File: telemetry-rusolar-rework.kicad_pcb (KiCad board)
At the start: 4 copper layers, 108.1 x 81.6 mm, 132 parts, among them IC1 TLV62569DBVR, J10 JP, J11 USB_B_Micro, J13 GR2, J14 GR1, J15 N_GR1, J19 Micro_SD_Card, J2 SPI, J3 MDT420E01001, J4 CAN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

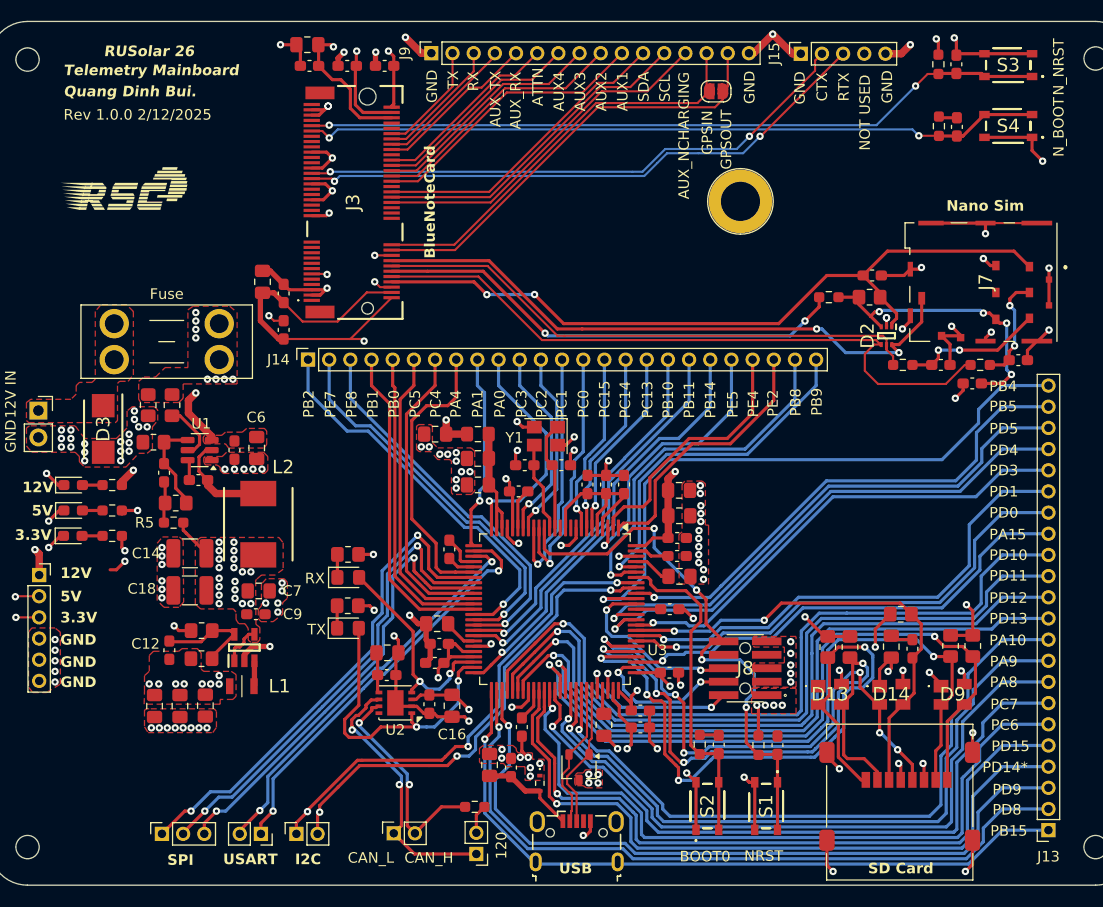
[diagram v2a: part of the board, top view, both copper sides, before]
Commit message: Fixed DRC errors
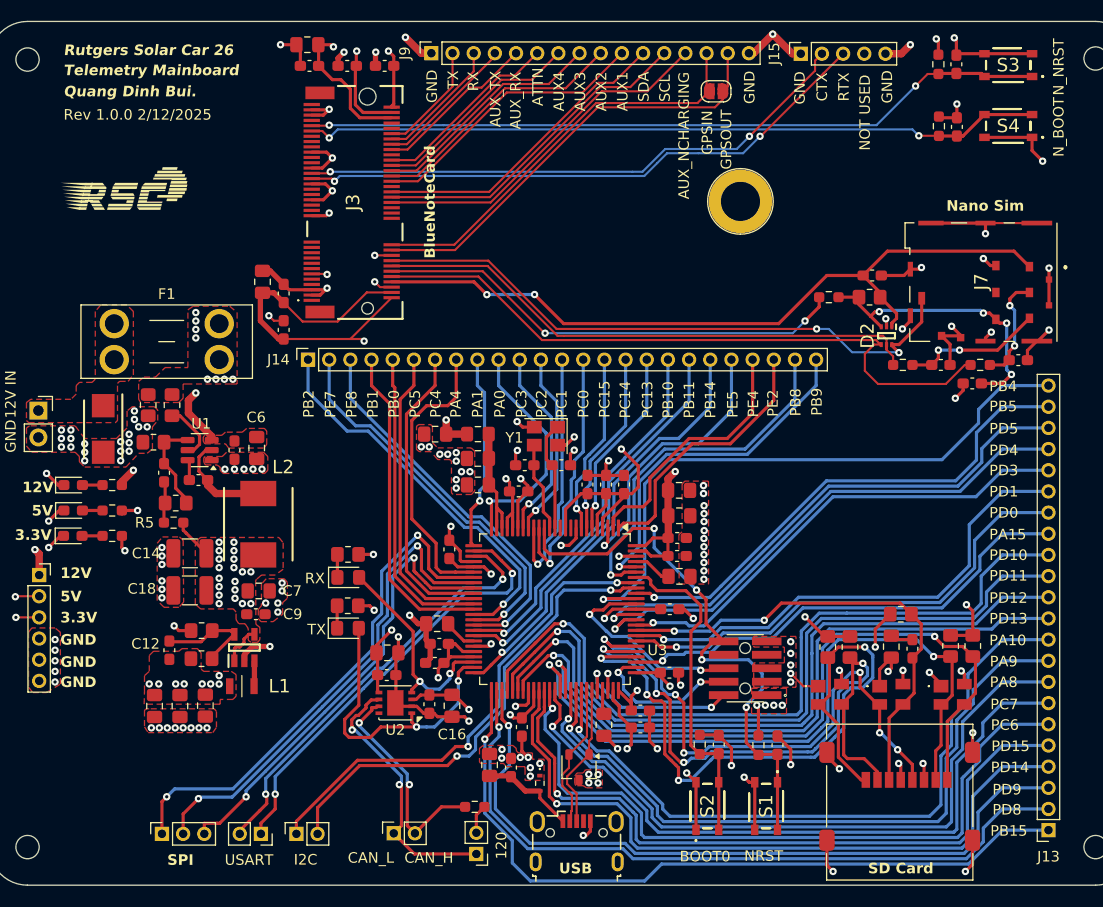
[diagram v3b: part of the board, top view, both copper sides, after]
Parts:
- renumbered Fuse to F1, USART to J1, I2C to J12
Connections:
- net PD14* renamed /PD14
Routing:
- net +3.3V Buck: track 153.9 -> 170.5 mm, vias 33 -> 38
- net GND: track 201.1 -> 212.4 mm, vias 149 -> 150
- net /USART2_TX: track 39.2 -> 41.8 mm
- net /PB15: track 68.4 -> 71.0 mm
- net /USART2_RX: track 38.3 -> 40.5 mm
- net /SWO: track 17.7 -> 19.7 mm
- net /SPI1_SCK: track 47.8 -> 49.6 mm
- net /NRST: track 53.0 -> 54.1 mm
- net /SPI1_MISO: track 45.1 -> 46.1 mm
- net /I2C1_SDA: vias 3 -> 2
- net /I2C1_SCL: vias 3 -> 2
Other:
- board text added: "I2C"
- board text added: "PD14"
- board text added: "Rutgers Solar Car 26"
- board text added: "USART"
- board text removed: "PD14*"
- board text removed: "RUSolar 26"

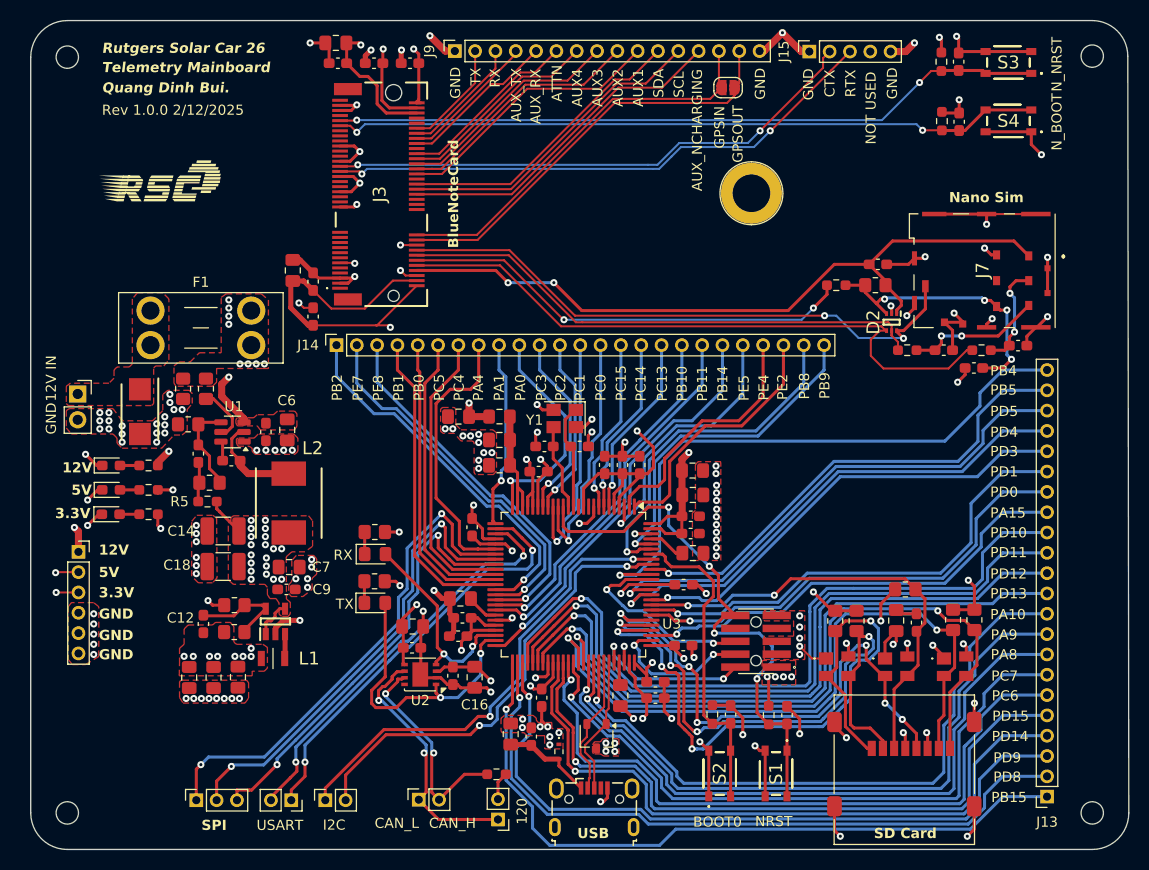
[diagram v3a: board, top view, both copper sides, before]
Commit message: Added ORing VBUS
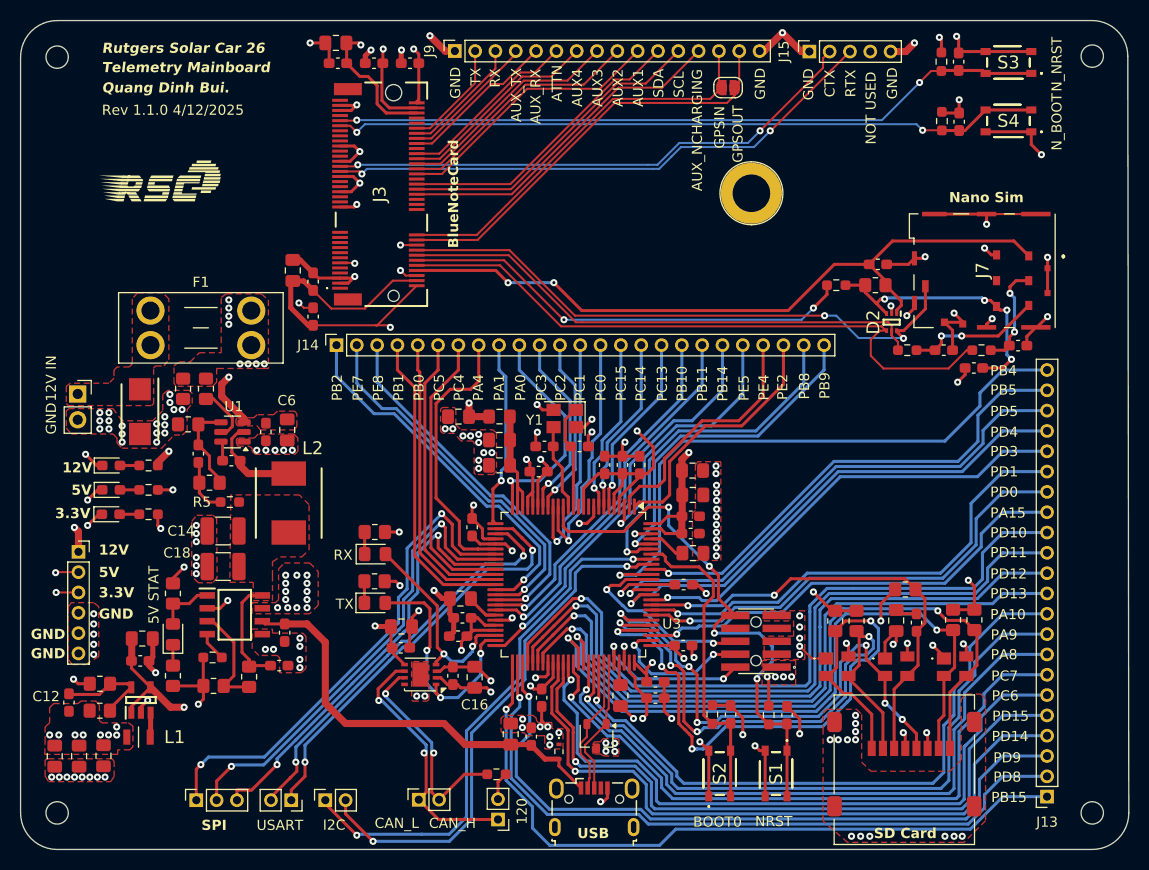
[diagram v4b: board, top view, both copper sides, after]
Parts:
- added C60: 100n, Capacitor_SMD:C_0603_1608Metric_Pad1.08x0.95mm_HandSolder, F.Cu at (45.5, 159.5)
- added C61: 100n, Capacitor_SMD:C_0603_1608Metric_Pad1.08x0.95mm_HandSolder, F.Cu at (46.0, 156.3)
- added D4: 5V_S, LED_SMD:LED_0805_2012Metric_Pad1.15x1.40mm_HandSolder, F.Cu at (35.0, 156.4)
- added IC2: TPS2113APW, SamacSys_Parts:NE555DR, F.Cu at (41.1, 154.5)
- added R10: 36k, Resistor_SMD:R_0805_2012Metric_Pad1.20x1.40mm_HandSolder, F.Cu at (39.0, 161.5)
- added R11: 500, Resistor_SMD:R_0603_1608Metric_Pad0.98x0.95mm_HandSolder, F.Cu at (38.9, 158.7)
- added R12: 10k, Resistor_SMD:R_0805_2012Metric_Pad1.20x1.40mm_HandSolder, F.Cu at (35.0, 152.4)
- added R31: 2k2, Resistor_SMD:R_0805_2012Metric_Pad1.20x1.40mm_HandSolder, F.Cu at (35.0, 160.5)
- added R9: 157k, Resistor_SMD:R_0805_2012Metric_Pad1.20x1.40mm_HandSolder, F.Cu at (42.5, 160.6)
- moved C7 16.1 mm to (32.0, 156.8)
- moved C9 16.0 mm to (31.8, 159.0)
- moved R6 15.3 mm to (27.8, 163.9)
- moved C21 15.3 mm to (28.2, 168.4)
- moved C12 15.3 mm to (24.8, 163.1)
- moved C15 15.3 mm to (23.4, 168.4)
- moved C20 15.3 mm to (25.8, 168.4)
- moved L1 15.3 mm to (31.6, 166.5)
- moved IC1 15.3 mm to (31.9, 162.9)
- moved R14 15.3 mm to (27.8, 161.3)
- moved R5 2.20 mm to (40.6, 143.4)
- moved C58 1.10 mm to (57.4, 157.8)
- moved C59 1.10 mm to (57.5, 155.7)
- moved H1 1.00 mm to (23.6, 99.6)
- moved H2 1.00 mm to (23.6, 174.0)
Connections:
- C26 pad 2: +5V Buck -> +5V
- C28 pad 2: +5V Buck -> +5V
- C29 pad 2: +5V Buck -> +5V
- C50 pad 2: +5V Buck -> +5V
- C7 pad 2: +5V Buck -> +5V
- C9 pad 1: +5V Buck -> +5V
- IC1 pad 1: +5V Buck -> +5V
- IC1 pad 4: +5V Buck -> +5V
- J3 pad 70: +5V Buck -> +5V
- J3 pad 72: +5V Buck -> +5V
- J3 pad 74: +5V Buck -> +5V
- J5 pad 2: +5V Buck -> +5V
- R29 pad 1: +5V Buck -> +5V
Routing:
- net +5V: track 0.00 -> 47.5 mm, vias 0 -> 20
- net VBUS: track 9.09 -> 42.1 mm
- net +5V Buck: track 40.1 -> 11.0 mm, vias 24 -> 0
- net Net-(IC2-VSNS): track 0.00 -> 10.7 mm
- net /I2C1_SCL: track 45.2 -> 52.1 mm
- net /I2C1_SDA: track 46.4 -> 53.2 mm
- net Net-(D4-A): track 0.00 -> 5.71 mm
- net /CAN2_TX: track 28.7 -> 25.0 mm, vias 2 -> 3
- net Net-(IC2-ILIM): track 0.00 -> 2.90 mm
- net Net-(D4-K): track 0.00 -> 2.05 mm
- net GND: track 212.4 -> 210.5 mm, vias 150 -> 165
- net Net-(C19-Pad1): track 3.94 -> 5.66 mm
- net +3.3V Buck: track 170.5 -> 169.8 mm
- net /SD1_D3: track 58.6 -> 58.0 mm
- added copper zone on F.Cu, net +5V
- added copper zone on In2.Cu, net +5V
- removed copper zone on In2.Cu, net +5V Buck
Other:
- board size 108.1 x 81.6 mm -> 109.1 x 81.6 mm
- board text added: "5V STAT"
- board text added: "Rev 1.1.0 4/12/2025"
- board text added: "https://github.com/bquangDinh/telemetry-board-rework"
- board text removed: "Rev 1.0.0 2/12/2025"

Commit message: Removed CAN TX/RX LED indicators
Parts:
- removed D5: TX, LED_SMD:LED_0805_2012Metric_Pad1.15x1.40mm_HandSolder
- removed D6: RX, LED_SMD:LED_0805_2012Metric_Pad1.15x1.40mm_HandSolder
- removed R7, R8: 1k5, Resistor_SMD:R_0805_2012Metric_Pad1.20x1.40mm_HandSolder
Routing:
- net /CAN2_TX: track 25.0 -> 10.2 mm, vias 3 -> 2
- net /CAN2_RX: track 20.6 -> 7.04 mm, vias 2 -> 0
- net +3.3V Buck: track 169.8 -> 176.7 mm
- net GND: track 210.5 -> 207.5 mm, vias 165 -> 163
- net Net-(D6-K): track 2.18 -> 0.00 mm
- net Net-(D5-K): track 2.12 -> 0.00 mm
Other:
- board text added: "Rev 1.1.1 4/12/2025"
- board text removed: "Rev 1.1.0 4/12/2025"

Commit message: Added LED indicators, USER LEDs, extended layout, fixed footprints
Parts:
- removed J19: Micro_SD_Card, Connector_Card:microSD_HC_Molex_47219-2001
- added C62: 100n, Capacitor_SMD:C_0603_1608Metric_Pad1.08x0.95mm_HandSolder, F.Cu at (83.4, 173.6)
- added D15: CAN_ERR, LED_SMD:LED_0805_2012Metric_Pad1.15x1.40mm_HandSolder, F.Cu at (53.5, 138.3)
- added D16: USER LED 1, LED_SMD:LED_0805_2012Metric_Pad1.15x1.40mm_HandSolder, F.Cu at (91.4, 142.1)
- added D17: USER LED 2, LED_SMD:LED_0805_2012Metric_Pad1.15x1.40mm_HandSolder, F.Cu at (91.4, 146.8)
- added D5: CAN_PWR, LED_SMD:LED_0805_2012Metric_Pad1.15x1.40mm_HandSolder, F.Cu at (53.7, 152.1)
- added D6: TX, LED_SMD:LED_0805_2012Metric_Pad1.15x1.40mm_HandSolder, F.Cu at (53.6, 147.4)
- added D7: RX, LED_SMD:LED_0805_2012Metric_Pad1.15x1.40mm_HandSolder, F.Cu at (53.6, 142.9)
- added FB1: FerriteBead, Inductor_SMD:L_0805_2012Metric_Pad1.05x1.20mm_HandSolder, F.Cu at (83.8, 175.5)
- added J16: 47219-2001, SamacSys_Parts:472192001, F.Cu at (106.1, 170.9)
- added R32: 1k5, Resistor_SMD:R_0603_1608Metric_Pad0.98x0.95mm_HandSolder, F.Cu at (55.8, 142.9)
- added R33: 1k5, Resistor_SMD:R_0603_1608Metric_Pad0.98x0.95mm_HandSolder, F.Cu at (55.8, 138.3)
- added R34: 1k5, Resistor_SMD:R_0603_1608Metric_Pad0.98x0.95mm_HandSolder, F.Cu at (92.9, 140.1)
- added R35: 1k5, Resistor_SMD:R_0603_1608Metric_Pad0.98x0.95mm_HandSolder, F.Cu at (92.9, 144.8)
- added R7: 1k5, Resistor_SMD:R_0603_1608Metric_Pad0.98x0.95mm_HandSolder, F.Cu at (55.8, 152.1)
- added R8: 1k5, Resistor_SMD:R_0603_1608Metric_Pad0.98x0.95mm_HandSolder, F.Cu at (55.8, 147.4)
- D10, D11, D12: footprint LED_SMD:LED_0603_1608Metric_Pad1.05x0.95mm_HandSolder -> LED_SMD:LED_0805_2012Metric_Pad1.15x1.40mm_HandSolder
- moved J11 2.80 mm to (76.5, 176.2)
- moved H2 2.50 mm to (23.6, 176.5)
- moved H3 2.50 mm to (125.5, 176.5)
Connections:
- net /PA4 renamed /PA4*
- net /PB1 renamed /PB1*
- net /PB2 renamed /PB2*
- net /PB5 renamed /PB5*
- net /PE2 renamed /PE2*
- J11 pad 6: unconnected-(J11-Shield-Pad6) -> Net-(J11-Shield)
- J14 pad 18: /PB10 -> PB10
- J14 pad 19: /PB11 -> PB11
- J14 pad 21: /PE5 -> PE5
- J3 pad 54: /blue-note-card/ATTN -> PE5
- J3 pad 62: /blue-note-card/RX -> PB10
- J3 pad 64: /blue-note-card/TX -> PB11
- J9 pad 2: /blue-note-card/TX -> PB11
- J9 pad 3: /blue-note-card/RX -> PB10
- J9 pad 6: /blue-note-card/ATTN -> PE5
- U3 pad 3: /PE5 -> PE5
- U3 pad 42: /PB10 -> PB10
- U3 pad 43: /PB11 -> PB11
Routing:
- net PB11: track 0.00 -> 101.0 mm, vias 0 -> 2
- net PB10: track 0.00 -> 98.4 mm, vias 0 -> 2
- net PE5: track 0.00 -> 95.4 mm, vias 0 -> 2
- net /PB11: track 37.2 -> 0.00 mm, vias 1 -> 0
- net /PB10: track 35.3 -> 0.00 mm, vias 1 -> 0
- net /PE5: track 26.3 -> 0.00 mm, vias 1 -> 0
- net Net-(J11-Shield): track 0.00 -> 20.1 mm
- net /blue-note-card/ATTN: track 17.9 -> 0.00 mm
- net +3.3V Buck: track 176.7 -> 191.3 mm
- net /blue-note-card/RX: track 12.1 -> 0.00 mm
- net /PA4*: track 27.2 -> 39.0 mm, vias 0 -> 2
- net /blue-note-card/TX: track 10.7 -> 0.00 mm
- net /PB2*: track 37.1 -> 46.5 mm, vias 1 -> 2
- net GND: track 207.5 -> 216.3 mm, vias 163 -> 176
- net /PE2*: track 25.4 -> 32.9 mm
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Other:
- board size 109.1 x 81.6 mm -> 109.1 x 84.1 mm
- board text added: "CAN_ERR"
- board text added: "CAN_PWR"
- board text added: "PA4*"
- board text added: "PA4* -> CAN_ERR"
- board text added: "PB1*"
- board text added: "PB1* -> TX"
- board text added: "PB10*"
- board text added: "PB10* -> USART3 TX"
- board text added: "PB11*"
- board text added: "PB11* -> USART3 RX"
- board text added: "PB2*"
- board text added: "PB2* -> RX"
- board text added: "PB5*"
- board text added: "PE2*"
- board text added: "PE2* -> USER LED 1"
- board text added: "PE5*"
- board text added: "PE5* -> USER LED 2"
- board text added: "SWD"
- board text added: "USER LED 1"
- board text added: "USER LED 2"
- board text added: "VBUS"
- board text removed: "PA4"
- board text removed: "PB1"
- board text removed: "PB10"
- board text removed: "PB11"
- board text removed: "PB2"
- board text removed: "PB5"
- board text removed: "PE2"
- board text removed: "PE5"

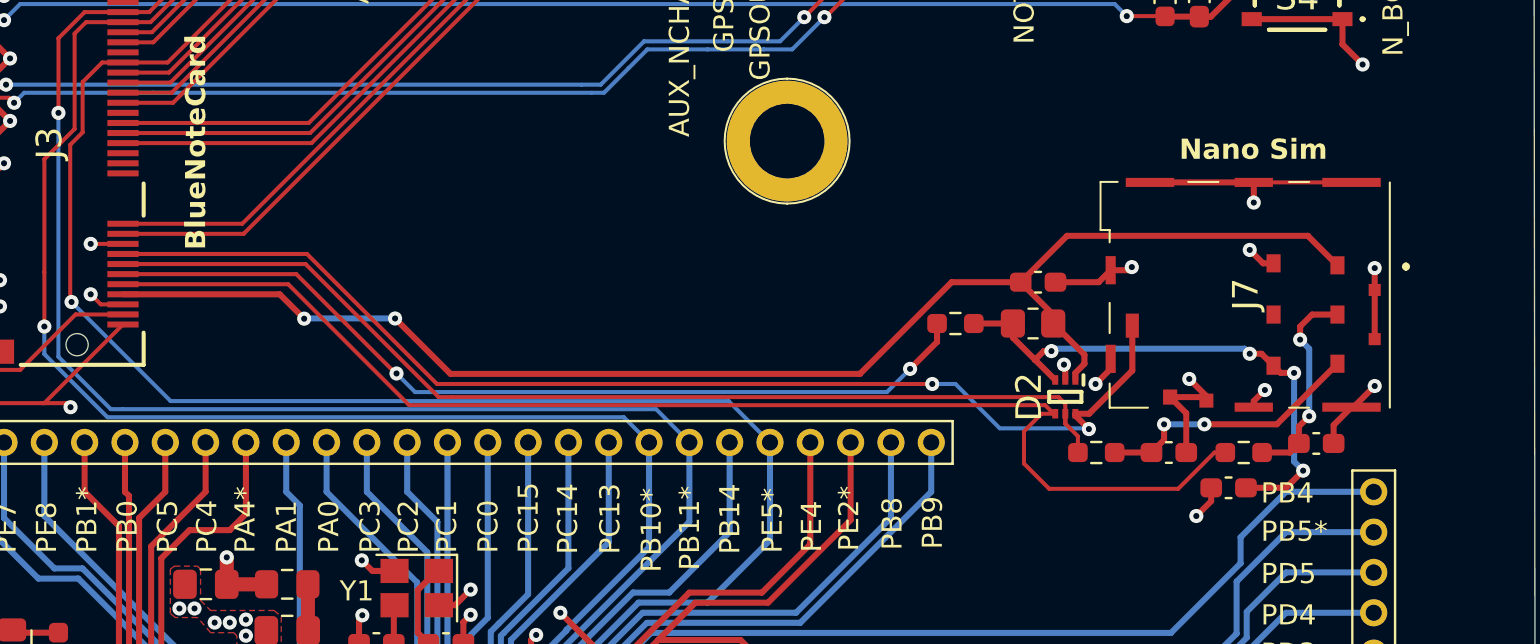
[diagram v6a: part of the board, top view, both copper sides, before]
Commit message: Relayout NanoSim component
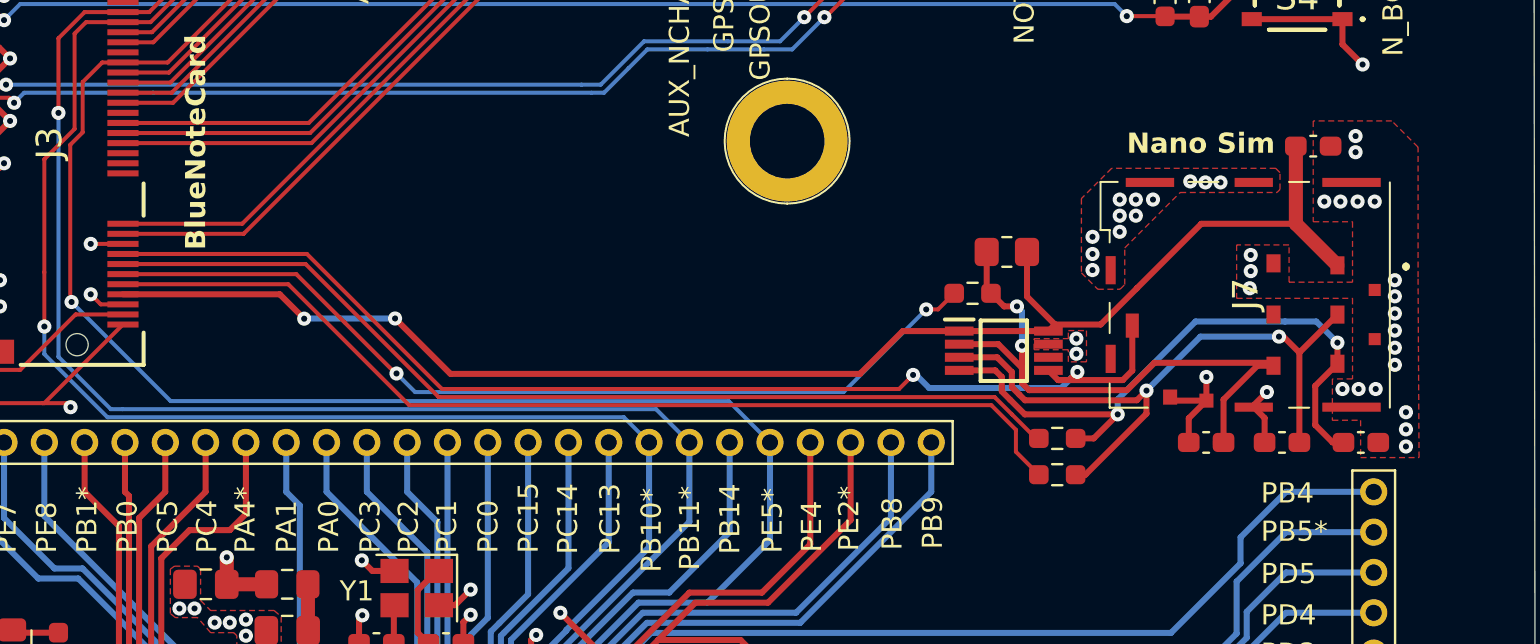
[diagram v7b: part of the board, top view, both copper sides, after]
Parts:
- removed D2: ESDLC5V0M5-TP, SamacSys_Parts:SOTFL50P160X60-6N
- added D18: DT6250-06MR-13, SamacSys_Parts:SOP65P490X110-8N, F.Cu at (102.7, 123.4)
- moved C22 15.2 mm to (118.0, 113.2)
- moved C25 9.54 mm to (120.4, 128.0)
- moved R19 9.32 mm to (105.3, 129.6)
- moved R17 3.78 mm to (102.8, 118.5), turned to 0 degrees
- moved C23 2.51 mm to (112.7, 128.0)
- moved R18 2.06 mm to (105.3, 127.8)
- moved R25 1.72 mm to (101.2, 120.5)
- moved C24 1.70 mm to (116.5, 128.0), turned to 0 degrees
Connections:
- C23 pad 2: Net-(D2-K_3) -> Net-(D18-I/O2)
- J7 pad C7: Net-(D2-K_3) -> Net-(D18-I/O2)
- R17 pad 1: /blue-note-card/SIM_VCC -> Net-(D18-I/O2)
- R17 pad 2: Net-(D2-K_3) -> /blue-note-card/SIM_VCC
- R25 pad 2: Net-(D2-K_3) -> Net-(D18-I/O2)
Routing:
- net Net-(D18-I/O2): track 0.00 -> 30.4 mm, vias 0 -> 2
- net Net-(D2-K_3): track 27.4 -> 0.00 mm, vias 4 -> 0
- net GND: track 216.3 -> 190.0 mm, vias 176 -> 203
- net Net-(D18-I/O3): track 10.3 -> 32.9 mm
- net Net-(D18-I/O4): track 13.3 -> 31.7 mm
- net /blue-note-card/SIM_RST: track 63.7 -> 50.0 mm
- net /blue-note-card/SIM_CLK: track 52.8 -> 49.0 mm
- net /blue-note-card/SIM_VCC: track 71.7 -> 73.9 mm
- net /blue-note-card/SIM_IO: track 44.8 -> 45.7 mm
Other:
- board text added: "PB5* -> USER LED 2"
- board text added: "PE5* -> ATTN"
- board text removed: "PE5* -> USER LED 2"
